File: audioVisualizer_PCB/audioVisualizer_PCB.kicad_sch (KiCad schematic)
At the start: 26 parts, among them J1 Microphone_Module, J2 USB_B_Micro, J3 SPI_MATRIX, J4 JTAG, U1 STM32F103C8Tx, U2 HT7333, Y1 8Mhz

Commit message: unfinished workflow and update on the TH of the PCB footprint
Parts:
- J3: footprint Connector_PinHeader_1.00mm:PinHeader_1x05_P1.00mm_Vertical -> Connector_PinSocket_2.54mm:PinSocket_1x05_P2.54mm_Vertical
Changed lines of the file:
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@@
 		(dnp no)
 		(property "Reference" "J3"
-			(at 178.308 87.376 0)
+			(at 177.292 108.712 0)
 			(effects
 				(font
@@
 		)
 		(property "Value" "SPI_MATRIX"
-			(at 179.07 90.17 0)
+			(at 178.054 106.68 0)
 			(effects
 				(font
@@
 			)
 		)
-		(property "Footprint" "Connector_PinHeader_1.00mm:PinHeader_1x05_P1.00mm_Vertical"
+		(property "Footprint" "Connector_PinSocket_2.54mm:PinSocket_1x05_P2.54mm_Vertical"
 			(at 177.8 99.06 0)
 			(effects

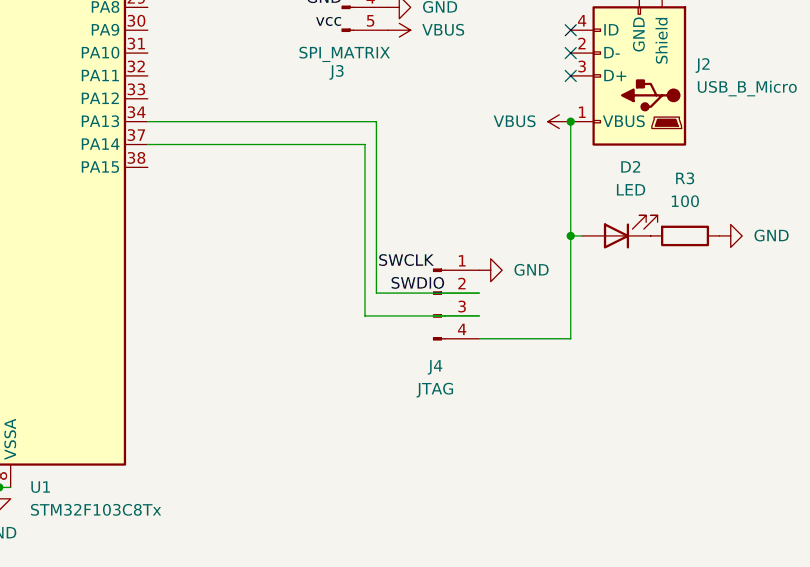
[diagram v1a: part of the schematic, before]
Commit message: Fixed headerpin diameter, updated workflow
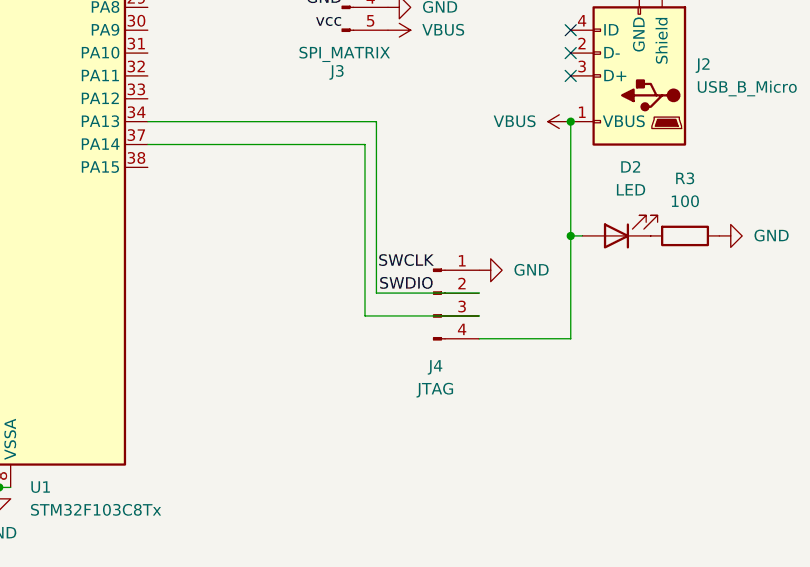
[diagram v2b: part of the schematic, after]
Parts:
- J1: footprint Connector_PinHeader_1.00mm:PinHeader_1x03_P1.00mm_Horizontal -> Connector_PinHeader_2.54mm:PinHeader_1x03_P2.54mm_Horizontal
- J4: footprint Connector_PinHeader_1.00mm:PinHeader_1x04_P1.00mm_Vertical -> Connector_PinHeader_2.54mm:PinHeader_1x04_P2.54mm_Vertical
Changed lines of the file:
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@@
 	)
 	(label "SWDIO"
-		(at 189.23 133.35 180)
+		(at 187.96 133.35 180)
 		(effects
 			(font
@@
 			)
 		)
-		(property "Footprint" "Connector_PinHeader_1.00mm:PinHeader_1x04_P1.00mm_Vertical"
+		(property "Footprint" "Connector_PinHeader_2.54mm:PinHeader_1x04_P2.54mm_Vertical"
 			(at 187.96 133.35 0)
 			(effects
@@
 			)
 		)
-		(property "Footprint" "Connector_PinHeader_1.00mm:PinHeader_1x03_P1.00mm_Horizontal"
+		(property "Footprint" "Connector_PinHeader_2.54mm:PinHeader_1x03_P2.54mm_Horizontal"
 			(at 176.53 83.82 0)
 			(effects
